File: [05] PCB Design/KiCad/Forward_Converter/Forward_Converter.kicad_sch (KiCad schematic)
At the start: 112 parts, among them J1 Conn_01x02_Pin, J2 Conn_01x02_Pin, J3 Conn_01x02_Pin, J4 Conn_01x02_Pin, J5 Conn_01x02_Pin, Q1 CSD19534Q5A, Q2 CSD19534Q5A, Q3 BSC320N20NS3G, Q4 BCX56, Q5 BC857, Q6 BCX56, T1 P0926NL, T2 EE30157-Custom, U1 LT1952EGN-1-PBF, U2 LTC3900ES8-PBF, U3 MC7812CDTRKG, U4 LT4430ES6-TRPBF, U5 TCMT1106

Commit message: Layout placement
Placement is almost complete connections to be completed.
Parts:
- removed L4: 22uH, Inductor_SMD:L_12x12mm_H6mm, symbol Device:L
- added L3: 10uH, Forward_Footprint:IND_VLS6045EX-100M-H, symbol Device:L
- J1: value Conn_01x02_Pin -> INPUT; footprint TerminalBlock_Phoenix:TerminalBlock_Phoenix_MKDS-1,5-2-5.08_1x02_P5.08mm_Horizontal -> Connector_Phoenix_MSTB:PhoenixContact_MSTBA_2,5_2-G-5,08_1x02_P5.08mm_Horizontal
- J2: renamed from J5; value Conn_01x02_Pin -> BIAS
- J3: renamed from J2; value Conn_01x02_Pin -> OUTPUT
- J4: renamed from J3; value Conn_01x02_Pin -> AUX
- J5: renamed from J4; value Conn_01x02_Pin -> 8V
- L1: renamed from L3; value 22uH -> 10uH; footprint Inductor_SMD:L_12x12mm_H6mm -> Forward_Footprint:IND_VLS6045EX-100M-H
- renumbered C5 to C1, C30 to C10, C25 to C11, C24 to C12, C23 to C13, C45 to C14, C42 to C15, C6 to C16, C2 to C17, C43 to C18, C44 to C19, C4 to C2, C31 to C20, C7 to C21, C32 to C22, C33 to C23, C8 to C24, C34 to C25, C9 to C26, C14 to C27, C15 to C28, C10 to C29, C22 to C3, C3 to C30, C37 to C31, C11 to C32, C38 to C33, C17 to C34, C41 to C35, C16 to C36, C20 to C37, C39 to C38, C1 to C39, C26 to C4, C12 to C41, C18 to C42, C13 to C43, C19 to C44, C35 to C45, C27 to C5, C28 to C6, C29 to C7, C36 to C8, C21 to C9, D10 to D1, D5 to D10, D9 to D2, D1 to D3, D8 to D4, D4 to D5, D3 to D8, D2 to D9, L1 to L2, Q3 to Q1, Q6 to Q2, Q5 to Q3, Q1 to Q4, Q2 to Q5, Q4 to Q6, R4 to R1, R9 to R10, R32 to R11, R30 to R12, R11 to R13, R33 to R14, R31 to R15, R29 to R16, R27 to R17, R12 to R18, R8 to R19, R7 to R2, R26 to R20, R25 to R21, R14 to R22, R15 to R23, R13 to R24, R16 to R25, R24 to R26, R17 to R27, R18 to R28, R19 to R29, R1 to R3, R20 to R30, R23 to R31, R28 to R32, R21 to R33, R22 to R34, R2 to R4, R10 to R5, R5 to R7, R34 to R8, R3 to R9, T2 to T1, T1 to T2, U5 to U2, U2 to U3, U3 to U5
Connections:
- net AUX: now also T1.2; no longer T1.4
- net GND: now also T1.1; no longer T1.5
- net Vin: now also T1.5; no longer T1.1
- net Vsw: now also T1.4; no longer T1.2
- net at C33.1, C37.1, C39.1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: now also L3.2
- net at D8.1 (K), D9.1 (K): now also L3.1

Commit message: [05] schematic with zero percent battery
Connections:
- net AUX: now also T1.4; no longer T1.2
- net GND: now also T1.5; no longer T1.1
- net GNDSEC: now also T1.6; no longer T1.10
- net VSEC+: now also T1.9; no longer T1.7
- net VSEC-: now also T1.10; no longer T1.8
- net Vaux: now also T1.7; no longer T1.9
- net Vin: now also T1.1; no longer T1.5
- net Vsw: now also T1.2; no longer T1.4
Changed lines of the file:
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@@
 		(pin "7"
 		)
-		(pin "8"
+		(pin "6"
 		)
 		(pin "2"

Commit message: Layout is updated
Close to the final result
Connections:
- net AUX: now also T1.2; no longer T1.4
- net GND: now also T1.1; no longer T1.5
- net Isense: now also R4.2
- net PGND: no longer R4.2
- net Vin: now also T1.5; no longer T1.1
- net Vsw: now also T1.4; no longer T1.2
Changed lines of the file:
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@@
 	)
 	(junction
-		(at 72.39 64.77)
-		(diameter 0)
-		(color 0 0 0 0)
-	)
-	(junction
 		(at 384.81 86.36)
 		(diameter 0)
@@
 	)
 	(junction
+		(at 72.39 55.88)
+		(diameter 0)
+		(color 0 0 0 0)
+	)
+	(junction
 		(at 168.91 31.75)
 		(diameter 0)
@@
 	(wire
 		(pts
+			(xy 60.96 55.88) (xy 72.39 55.88)
+		)
+		(stroke
+			(width 0)
+			(type default)
+		)
+	)
+	(wire
+		(pts
 			(xy 377.19 120.65) (xy 377.19 123.19)
 		)
@@
 	(wire
 		(pts
-			(xy 60.96 64.77) (xy 72.39 64.77)
-		)
-		(stroke
-			(width 0)
-			(type default)
-		)
-	)
-	(wire
-		(pts
 			(xy 175.26 24.13) (xy 181.61 24.13)
 		)
@@
 	(wire
 		(pts
-			(xy 60.96 55.88) (xy 60.96 64.77)
-		)
-		(stroke
-			(width 0)
-			(type default)
-		)
-	)
-	(wire
-		(pts
 			(xy 127 80.01) (xy 147.32 80.01)
 		)
@@
 	(wire
 		(pts
-			(xy 72.39 63.5) (xy 72.39 64.77)
+			(xy 72.39 53.34) (xy 72.39 55.88)
 		)
 		(stroke
@@
 	(wire
 		(pts
-			(xy 72.39 53.34) (xy 72.39 55.88)
-		)
-		(stroke
-			(width 0)
-			(type default)
-		)
-	)
-	(wire
-		(pts
 			(xy 90.17 242.57) (xy 90.17 248.92)
 		)
@@
 		)
 		(stroke
+			(width 0)
+			(type default)
+		)
+	)
+	(wire
+		(pts
+			(xy 72.39 63.5) (xy 72.39 64.77)
+		)
+		(stroke

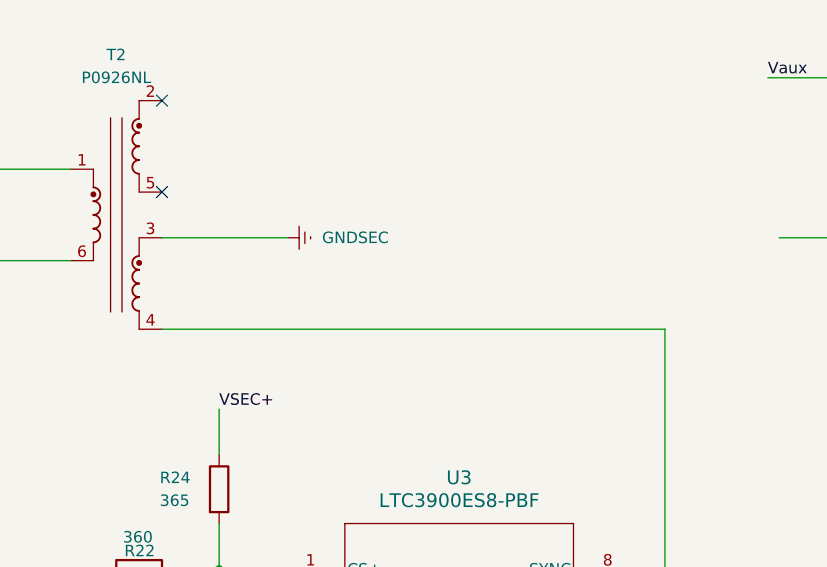
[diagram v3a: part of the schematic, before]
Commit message: [05] Sync Resistor added
Sync Resistor added
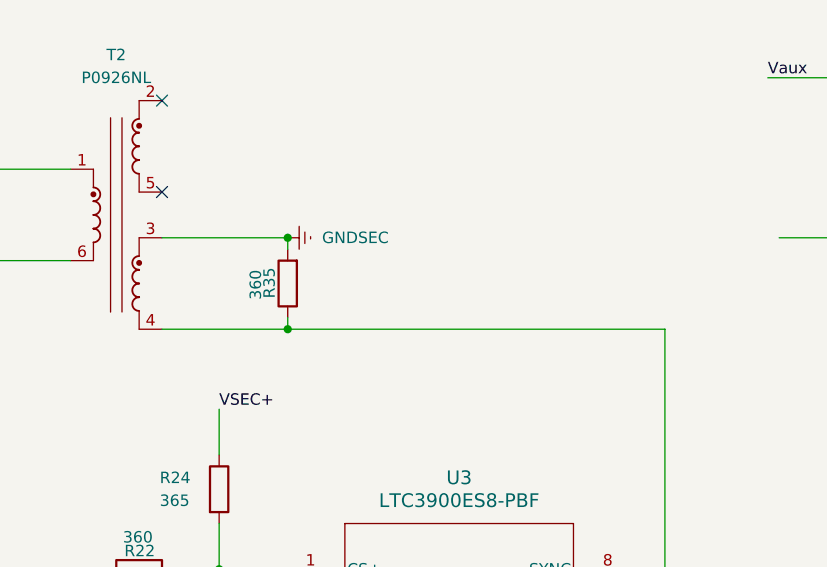
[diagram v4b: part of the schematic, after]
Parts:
- added R35: 360, Resistor_SMD:R_1206_3216Metric, symbol Device:R
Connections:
- net GNDSEC: now also R35.2
- net at T2.4, U3.8 (SYNC): now also R35.1
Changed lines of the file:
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@@
 	)
 	(junction
+		(at 233.68 104.14)
+		(diameter 0)
+		(color 0 0 0 0)
+	)
+	(junction
 		(at 147.32 80.01)
 		(diameter 0)
@@
 	)
 	(junction
+		(at 233.68 114.3)
+		(diameter 0)
+		(color 0 0 0 0)
+	)
+	(junction
 		(at 153.67 134.62)
 		(diameter 0)
@@
 	(wire
 		(pts
+			(xy 233.68 105.41) (xy 233.68 104.14)
+		)
+		(stroke
+			(width 0)
+			(type default)
+		)
+	)
+	(wire
+		(pts
 			(xy 133.35 142.24) (xy 168.91 142.24)
 		)
@@
 	(wire
 		(pts
-			(xy 219.71 114.3) (xy 275.59 114.3)
+			(xy 219.71 114.3) (xy 233.68 114.3)
 		)
 		(stroke
@@
 	(wire
 		(pts
+			(xy 233.68 113.03) (xy 233.68 114.3)
+		)
+		(stroke
+			(width 0)
+			(type default)
+		)
+	)
+	(wire
+		(pts
 			(xy 133.35 147.32) (xy 137.16 147.32)
 		)
@@
 	(wire
 		(pts
+			(xy 233.68 114.3) (xy 275.59 114.3)
+		)
+		(stroke
+			(width 0)
+			(type default)
+		)
+	)
+	(wire
+		(pts
 			(xy 252.73 50.8) (xy 252.73 54.61)
 		)
@@
 					(unit 1)
 				)
+			)
+		)
+	)
+	(symbol
+		(lib_id "Device:R")
+		(at 233.68 109.22 180)
+		(unit 1)
+		(exclude_from_sim no)
+		(in_bom yes)
+		(on_board yes)
+		(dnp no)
+		(property "Reference" "R35"
+			(at 231.648 107.442 90)
+			(effects
+				(font
+					(size 1.27 1.27)
+				)
+				(justify left)
+			)
+		)
+		(property "Value" "360"
+			(at 230.124 107.696 90)
+			(effects
+				(font
+					(size 1.27 1.27)
+				)
+				(justify left)
+			)
+		)
+		(property "Footprint" "Resistor_SMD:R_1206_3216Metric"
+			(at 235.458 109.22 90)
+			(effects
+				(font
+					(size 1.27 1.27)
+				)
+				(hide yes)
+			)
+		)
+		(property "Datasheet" "~"
+			(at 233.68 109.22 0)
+			(effects
+				(font
+					(size 1.27 1.27)
+				)
+				(hide yes)
+			)
+		)
+		(property "Description" "Resistor"
+			(at 233.68 109.22 0)
+			(effects
+				(font
+					(size 1.27 1.27)
+				)
+				(hide yes)
+			)
+		)
+		(pin "1"
+		)
+		(pin "2"
+		)
+		(instances
+			(project "Forward_Converter"
+				(path "/b41a78d0-7732-4b67-b62d-4c11cdfa1967"
+					(reference "R35")
+					(unit 1)
+				)
